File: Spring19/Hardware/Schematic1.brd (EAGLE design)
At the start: 73.6 x 59.4 mm, 19 parts, among them X1 SSW-101-02-G-D

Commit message: Adjust cap1188 footprint and add some bottom routes
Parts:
- removed CAP1188: (no value), pinhead:2X13
- added CAPLEFT, CAPRIGHT: (no value), con-lstb:MA13-1
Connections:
- net GND: now also CAPLEFT.10; no longer CAP1188.7
- net N$7: now also CAPLEFT.13; no longer CAP1188.1
- net N$8: now also CAPLEFT.12; no longer CAP1188.3
- net VCC: now also CAPLEFT.11; no longer CAP1188.5
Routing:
- net VCC: track 65.7 -> 103.6 mm
- net GND: track 179.7 -> 205.6 mm
- net N$8: track 37.4 -> 46.0 mm
- net N$7: track 29.6 -> 35.9 mm
- net N$5: track 37.8 -> 36.1 mm
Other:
- board size 73.6 x 59.4 mm -> 77.5 x 60.6 mm

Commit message: Adjust routes
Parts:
- moved X1 10.2 mm to (99.1, 44.5)
- moved RELAYLEFT 3.81 mm to (101.6, 63.5)
- moved RELAYRIGHT 3.81 mm to (101.6, 54.6)
- moved R5 1.80 mm to (105.4, 68.6)
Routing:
- net GND: track 205.6 -> 176.8 mm
- net N$6: track 24.1 -> 31.7 mm
- net N$13: track 4.34 -> 10.7 mm
- net N$11: track 7.93 -> 12.8 mm
- net N$9: track 31.8 -> 34.8 mm
- net VCC: track 103.6 -> 101.5 mm
- net N$14: track 17.0 -> 18.2 mm

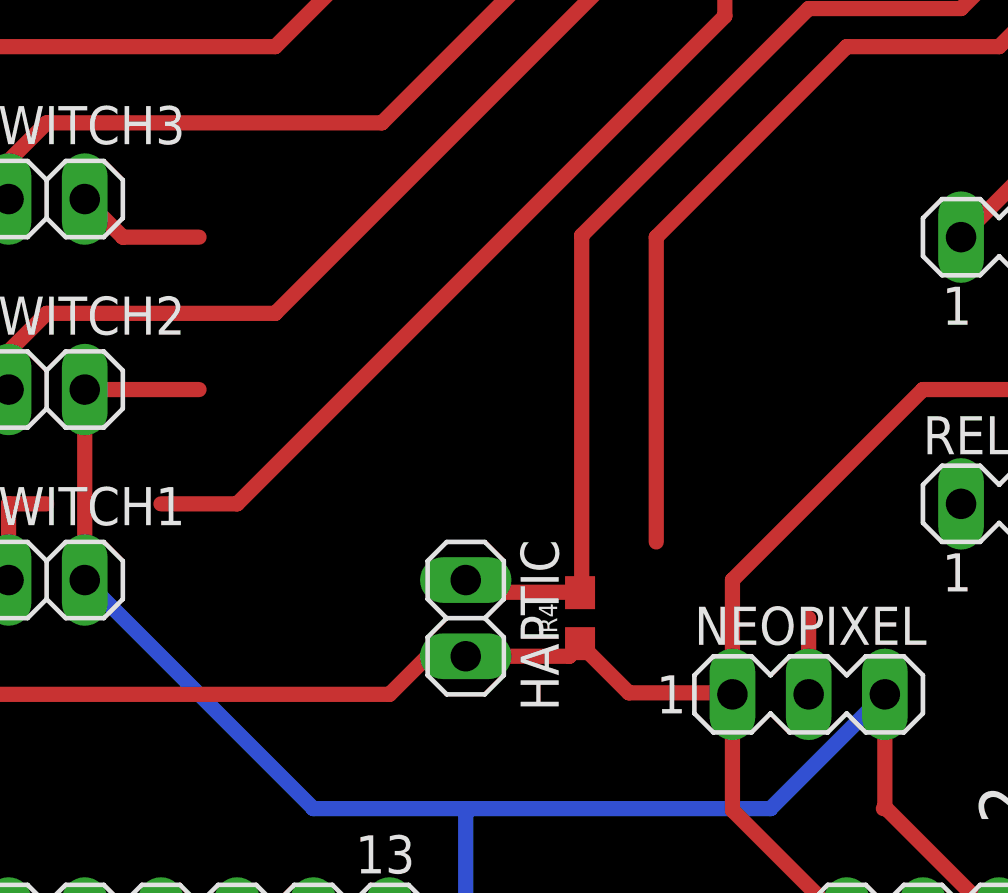
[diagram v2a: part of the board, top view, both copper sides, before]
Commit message: airwire route thickness
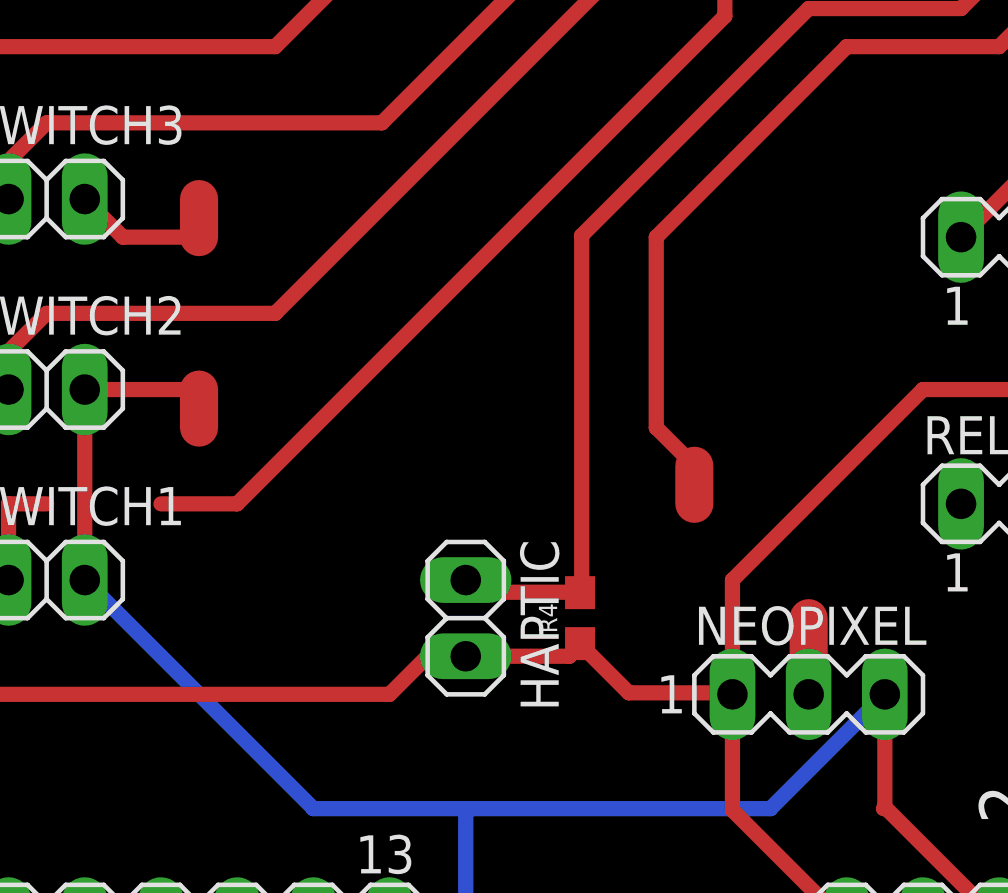
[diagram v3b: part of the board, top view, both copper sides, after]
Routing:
- net VCC: track 101.5 -> 104.0 mm
- net N$6: track 31.7 -> 31.0 mm
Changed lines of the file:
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@@
 <wire x1="69.85" y1="25.4" x2="77.47" y2="33.02" width="0.508" layer="16"/>
 <wire x1="77.47" y1="33.02" x2="77.47" y2="44.45" width="0.508" layer="16"/>
+<wire x1="68.58" y1="63.5" x2="68.58" y2="64.77" width="1.27" layer="1"/>
+<wire x1="68.58" y1="58.42" x2="68.58" y2="57.15" width="1.27" layer="1"/>
 <wire x1="68.58" y1="58.42" x2="68.58" y2="63.5" width="0" layer="19" extent="1-1"/>
 </signal>
@@
 <contactref element="IC1" pad="18"/>
 <wire x1="89.0016" y1="48.3108" x2="88.9" y2="48.26" width="0.1524" layer="16"/>
-<wire x1="88.9" y1="48.26" x2="88.9" y2="50.8" width="0.508" layer="1"/>
+<wire x1="88.9" y1="48.26" x2="88.9" y2="50.8" width="1.27" layer="1"/>
 <wire x1="97.79" y1="73.66" x2="97.79" y2="72.39" width="0.508" layer="1"/>
 <wire x1="90.17" y1="69.85" x2="83.82" y2="63.5" width="0.508" layer="1"/>
-<wire x1="83.82" y1="63.5" x2="83.82" y2="53.34" width="0.508" layer="1"/>
 <wire x1="97.79" y1="72.39" x2="95.25" y2="69.85" width="0.508" layer="1"/>
 <wire x1="95.25" y1="69.85" x2="90.17" y2="69.85" width="0.508" layer="1"/>
-<wire x1="83.82" y1="53.34" x2="88.9" y2="50.8" width="0" layer="19" extent="1-1"/>
+<wire x1="83.82" y1="63.5" x2="83.82" y2="57.15" width="0.508" layer="1"/>
+<wire x1="83.82" y1="57.15" x2="85.09" y2="55.88" width="0.508" layer="1"/>
+<wire x1="85.09" y1="55.88" x2="85.09" y2="54.61" width="1.27" layer="1"/>
+<wire x1="85.09" y1="54.61" x2="88.9" y2="50.8" width="0" layer="19" extent="1-1"/>
 </signal>
 <signal name="N$9">

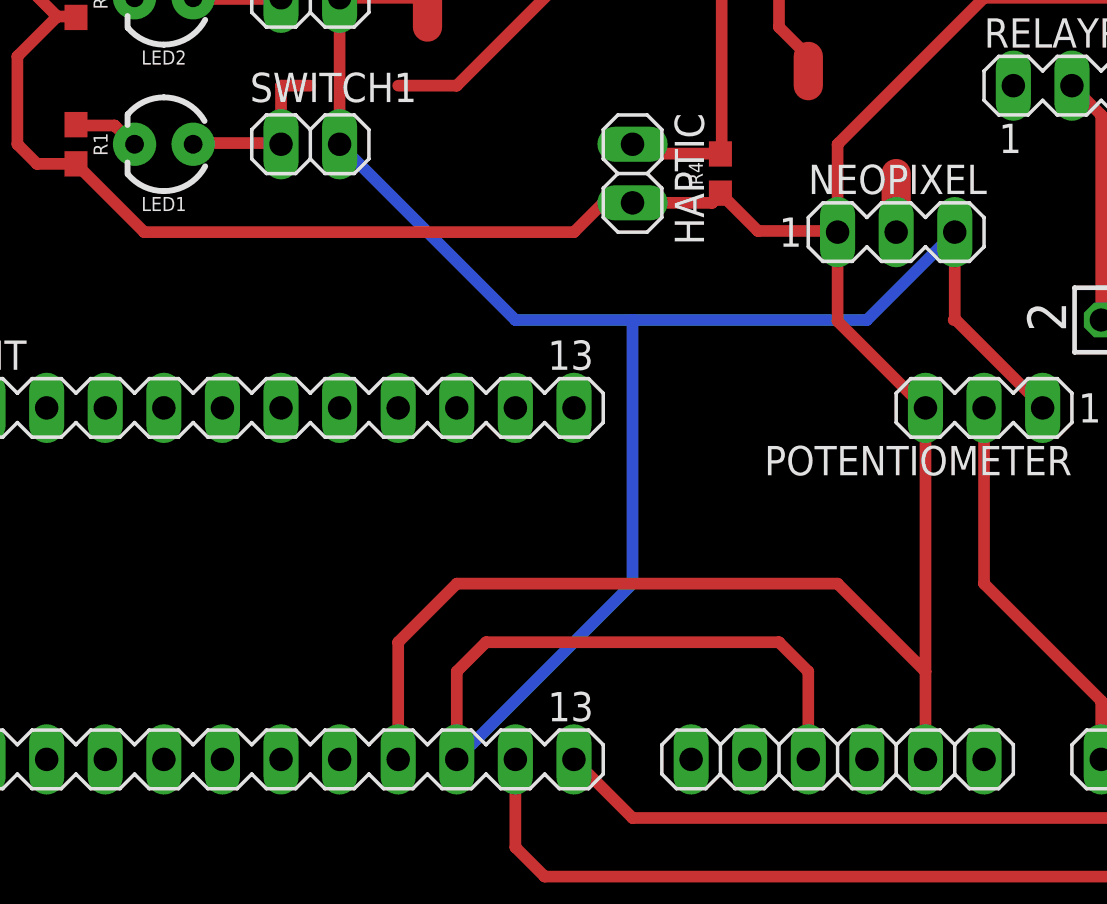
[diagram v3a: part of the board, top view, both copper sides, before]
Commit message: Switch back to airwires; single sided boards
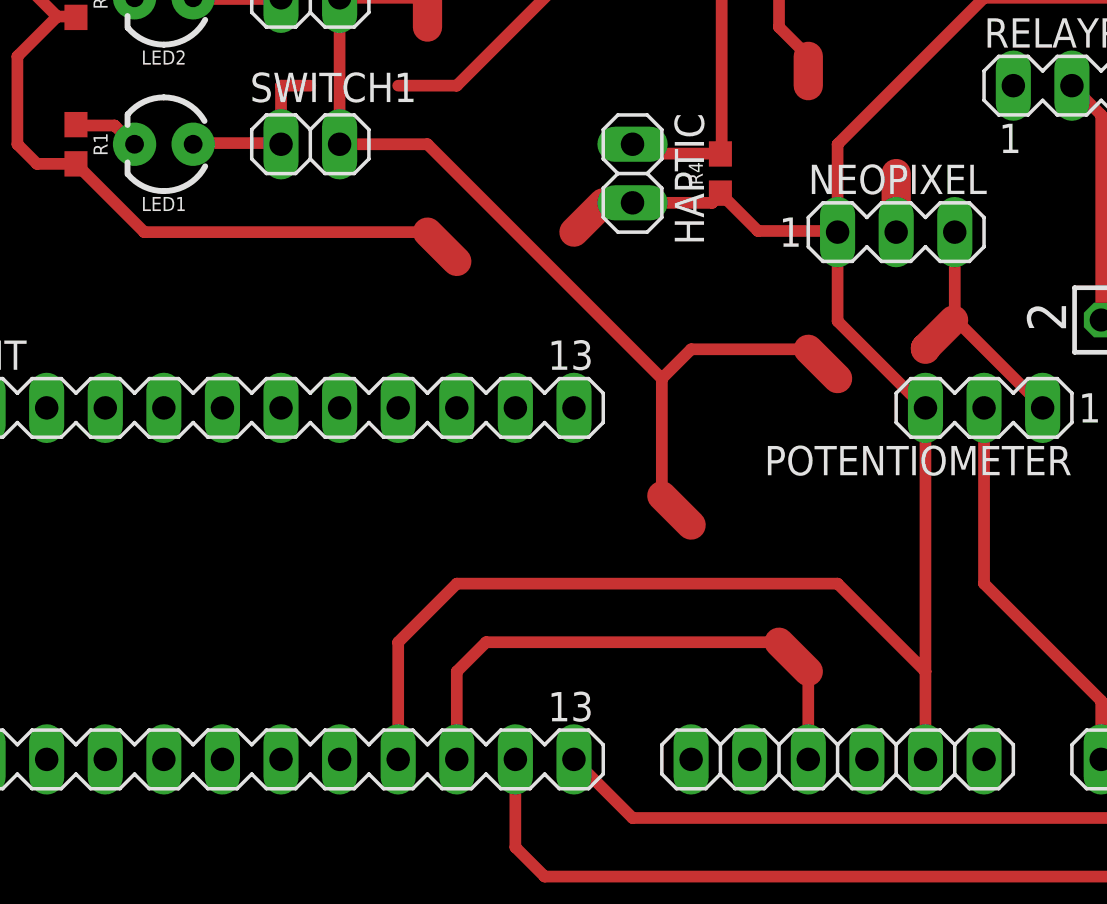
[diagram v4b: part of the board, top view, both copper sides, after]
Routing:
- net VCC: track 104.0 -> 85.9 mm
- net GND: track 176.8 -> 172.3 mm
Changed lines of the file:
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@@
 <contactref element="CAPLEFT" pad="10"/>
 <wire x1="53.34" y1="51.22" x2="56.3" y2="48.26" width="0.508" layer="1"/>
-<wire x1="56.3" y1="48.26" x2="74.93" y2="48.26" width="0.508" layer="1"/>
-<wire x1="74.93" y1="48.26" x2="76.2" y2="49.53" width="0.508" layer="1"/>
+<wire x1="74.93" y1="48.26" x2="76.2" y2="49.53" width="1.27" layer="1"/>
 <wire x1="90.17" y1="40.64" x2="90.17" y2="29.21" width="0.508" layer="1"/>
 <wire x1="90.17" y1="29.21" x2="90.17" y2="25.4" width="0.508" layer="1"/>
@@
 <wire x1="105.41" y1="58.42" x2="92.71" y2="58.42" width="0.508" layer="1"/>
 <wire x1="92.71" y1="58.42" x2="86.36" y2="52.07" width="0.508" layer="1"/>
+<wire x1="56.3" y1="48.26" x2="68.58" y2="48.26" width="0.508" layer="1"/>
+<wire x1="68.58" y1="48.26" x2="69.85" y2="46.99" width="1.27" layer="1"/>
 <wire x1="90.0684" y1="25.4508" x2="87.63" y2="25.4" width="0" layer="19" extent="1-1"/>
+<wire x1="69.85" y1="46.99" x2="74.93" y2="48.26" width="0" layer="19" extent="1-1"/>
 </signal>
 <signal name="+3V3">
@@
 <wire x1="69.85" y1="29.21" x2="71.12" y2="30.48" width="0.508" layer="1"/>
 <wire x1="71.12" y1="30.48" x2="83.82" y2="30.48" width="0.508" layer="1"/>
-<wire x1="83.82" y1="30.48" x2="85.09" y2="29.21" width="0.508" layer="1"/>
+<wire x1="83.82" y1="30.48" x2="85.09" y2="29.21" width="1.27" layer="1"/>
 <wire x1="85.09" y1="29.21" x2="85.09" y2="25.4" width="0.508" layer="1"/>
-<wire x1="64.77" y1="52.07" x2="72.39" y2="44.45" width="0.508" layer="16"/>
-<wire x1="87.63" y1="44.45" x2="91.44" y2="48.26" width="0.508" layer="16"/>
-<wire x1="72.39" y1="44.45" x2="77.47" y2="44.45" width="0.508" layer="16"/>
-<wire x1="77.47" y1="44.45" x2="87.63" y2="44.45" width="0.508" layer="16"/>
-<wire x1="69.85" y1="25.4" x2="77.47" y2="33.02" width="0.508" layer="16"/>
-<wire x1="77.47" y1="33.02" x2="77.47" y2="44.45" width="0.508" layer="16"/>
 <wire x1="68.58" y1="63.5" x2="68.58" y2="64.77" width="1.27" layer="1"/>
 <wire x1="68.58" y1="58.42" x2="68.58" y2="57.15" width="1.27" layer="1"/>
-<wire x1="68.58" y1="58.42" x2="68.58" y2="63.5" width="0" layer="19" extent="1-1"/>
+<wire x1="64.77" y1="52.07" x2="68.58" y2="52.07" width="0.508" layer="1"/>
+<wire x1="68.58" y1="52.07" x2="78.74" y2="41.91" width="0.508" layer="1"/>
+<wire x1="78.74" y1="41.91" x2="78.74" y2="36.83" width="0.508" layer="1"/>
+<wire x1="78.74" y1="36.83" x2="80.01" y2="35.56" width="1.27" layer="1"/>
+<wire x1="78.74" y1="41.91" x2="80.01" y2="43.18" width="0.508" layer="1"/>
+<wire x1="85.09" y1="43.18" x2="86.36" y2="41.91" width="1.27" layer="1"/>
+<wire x1="80.01" y1="43.18" x2="85.09" y2="43.18" width="0.508" layer="1"/>
+<wire x1="91.3892" y1="44.45" x2="90.17" y2="43.2308" width="1.27" layer="1"/>
+<wire x1="90.17" y1="43.2308" x2="90.17" y2="43.18" width="1.27" layer="1"/>
+<wire x1="86.36" y1="41.91" x2="90.17" y2="43.18" width="0" layer="19" extent="1-1"/>
+<wire x1="68.58" y1="63.5" x2="68.58" y2="58.42" width="0" layer="19" extent="1-1"/>
+<wire x1="83.82" y1="30.48" x2="80.01" y2="35.56" width="0" layer="19" extent="1-1"/>
 </signal>
 <signal name="N$7">

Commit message: adjust routes again
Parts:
- moved HAPTIC 1.27 mm to (78.7, 50.8)
- moved R4 1.27 mm to (82.5, 50.8)
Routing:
- net N$5: track 36.1 -> 34.8 mm
- net GND: track 172.3 -> 171.2 mm
- net N$9: track 34.8 -> 34.0 mm

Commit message: PCB for etching
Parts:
- removed CAPLEFT, CAPRIGHT: (no value), con-lstb:MA13-1
- removed SWITCH1, SWITCH2, SWITCH3: (no value), pinhead:1X02
- added SV1, SV2, SV3: (no value), con-lstb:MA03-1
- added SV4: (no value), con-lstb:MA04-1
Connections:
- net GND: now also SV4.4; no longer CAPLEFT.10
- net N$10: now also SV3.1; no longer SWITCH3.1
- net N$4: now also SV1.1; no longer SWITCH2.1
- net N$5: now also SV2.1; no longer SWITCH1.1
- net N$7: now also SV4.1; no longer CAPLEFT.13
- net N$8: now also SV4.2; no longer CAPLEFT.12
- net VCC: now also SV1.2, SV2.2, SV3.2, SV4.3; no longer CAPLEFT.11, SWITCH1.2, SWITCH2.2, SWITCH3.2
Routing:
- net N$8: track 46.0 -> 9.72 mm
- net N$7: track 35.9 -> 8.98 mm
- net GND: track 171.2 -> 175.5 mm
- net N$5: track 34.8 -> 37.7 mm
- net VCC: track 86.2 -> 87.7 mm
- net N$4: track 32.9 -> 31.4 mm
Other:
- board size 77.5 x 60.6 mm -> 73.6 x 59.4 mm

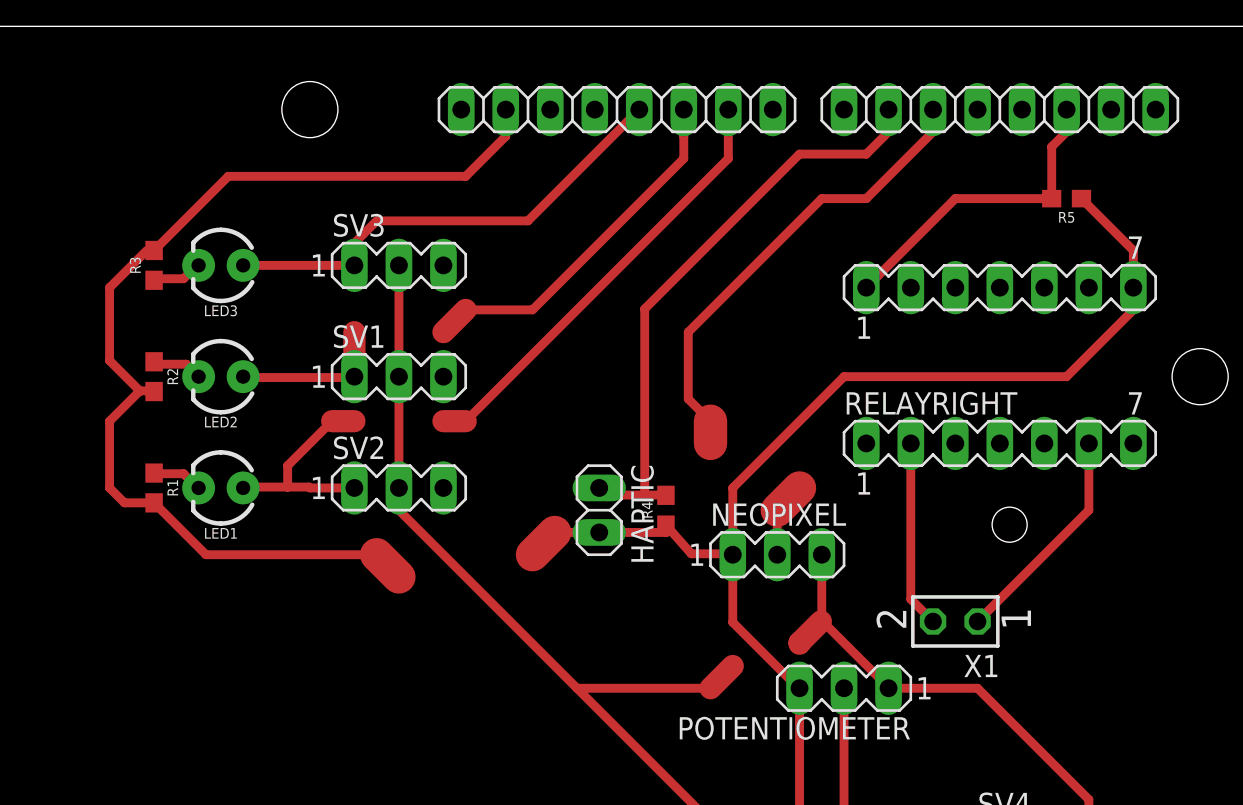
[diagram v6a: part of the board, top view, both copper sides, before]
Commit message: Switch relay direction
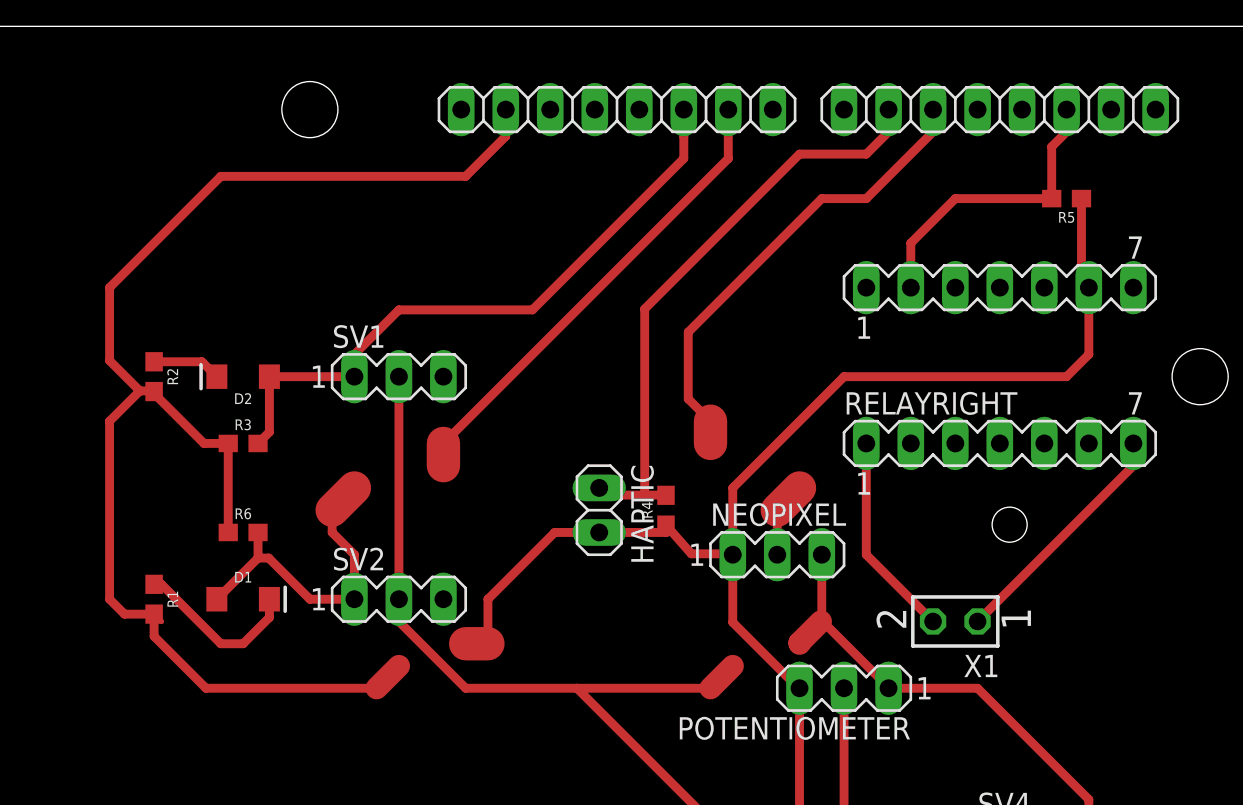
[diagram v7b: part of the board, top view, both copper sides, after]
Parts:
- removed LED1, LED2, LED3: (no value), SparkFun-LED:LED_3MM
- removed SV3: (no value), con-lstb:MA03-1
- added D1, D2: GREEN, SparkFun-LED:LED-1206
- added R6: 1k, SparkFun-Resistors:0603
- moved R3 11.4 mm to (58.4, 54.6), turned to 0 degrees
- moved R1 6.35 mm to (53.3, 45.7)
- moved SV2 6.35 mm to (67.3, 45.7)
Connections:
- removed net N$10: IC1.24, LED3.A, SV3.1
- removed net N$3: LED3.K, R3.1
- net GND: now also R3.1, R6.1, RELAYLEFT.6; no longer R3.2, RELAYLEFT.7
- net N$1: now also D1.C; no longer LED1.K
- net N$11: now also RELAYRIGHT.7; no longer RELAYRIGHT.6
- net N$13: now also RELAYRIGHT.1; no longer RELAYRIGHT.2
- net N$14: now also RELAYLEFT.2; no longer RELAYLEFT.1
- net N$2: now also D2.C; no longer LED2.K
- net N$4: now also D2.A, R3.2; no longer LED2.A
- net N$5: now also D1.A, R6.2; no longer LED1.A
- net VCC: no longer SV3.2
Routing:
- net N$10: track 27.5 -> 0.00 mm
- net GND: track 175.5 -> 198.4 mm
- net N$5: track 37.7 -> 45.7 mm
- net N$4: track 31.4 -> 38.3 mm
- net N$1: track 2.90 -> 9.65 mm
- net N$3: track 2.94 -> 0.00 mm
- net VCC: track 87.7 -> 85.0 mm
- net N$13: track 10.7 -> 11.7 mm
- net N$11: track 12.8 -> 13.8 mm
- net N$14: track 18.1 -> 17.1 mm
- net N$2: track 2.97 -> 3.93 mm

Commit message: for etching 4.3.19
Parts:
- added X2: SSW-101-02-G-D, con-samtec:SSW-101-02-G-D
- moved SV1 5.68 mm to (69.8, 63.5)
- moved D2 5.08 mm to (58.4, 63.5)
- moved SV2 2.54 mm to (69.8, 45.7)
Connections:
- net GND: now also X2.2
- net VCC: now also X2.1
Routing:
- net GND: track 198.4 -> 176.7 mm
- net VCC: track 85.0 -> 98.2 mm
- net N$4: track 38.3 -> 41.4 mm
- net N$6: track 31.3 -> 28.8 mm
- net N$9: track 34.0 -> 31.8 mm
- net N$2: track 3.93 -> 5.71 mm
- net N$5: track 45.7 -> 47.2 mm
